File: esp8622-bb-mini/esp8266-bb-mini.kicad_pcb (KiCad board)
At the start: 2 copper layers, 34.3 x 31.8 mm, 17 parts, among them J1 Conn_01x02_Male, J2 Conn_01x04_Male, J3 Conn_01x04_Male, J4 Conn_01x04_Male, J5 Conn_01x04_Male, U1 LP38693MP-3.3, U2 ESP-12F

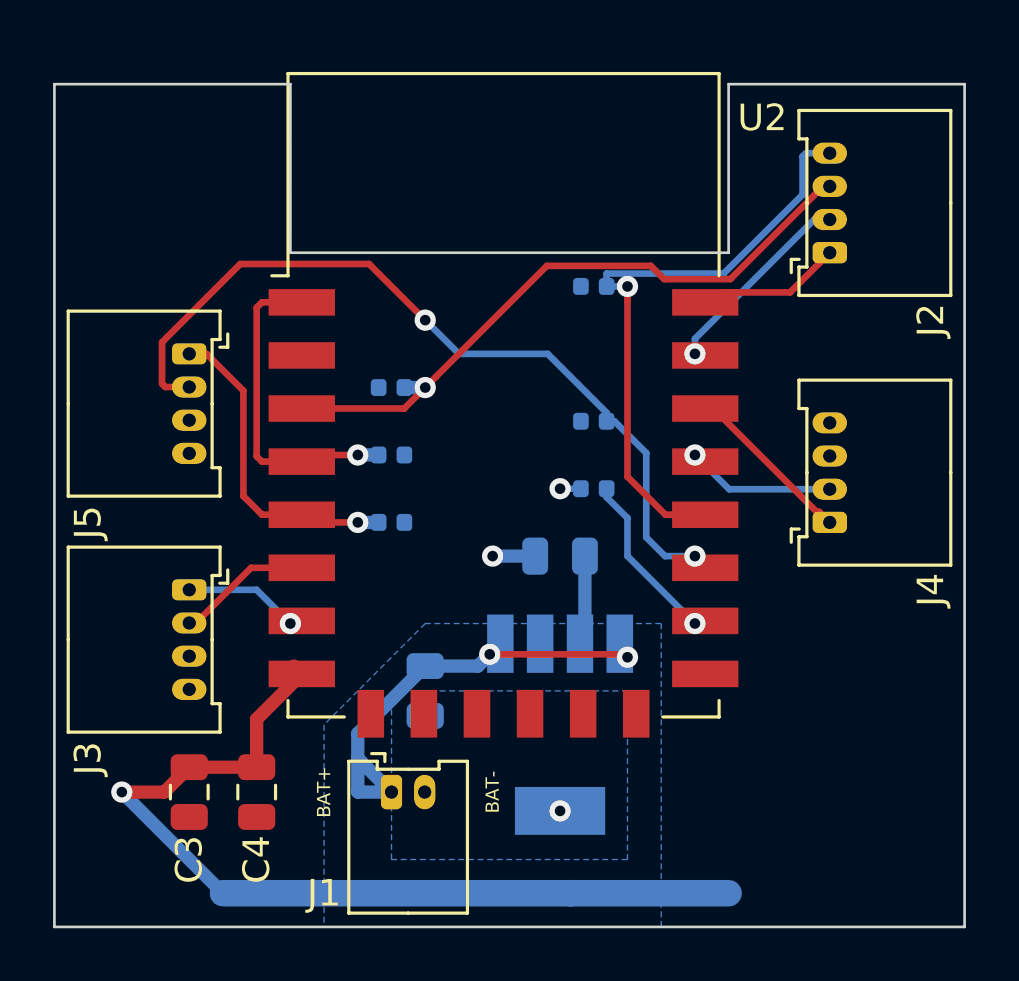
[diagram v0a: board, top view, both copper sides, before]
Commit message: brd: misc changes
- re-add mounting holes
- fix copper pour keepout around input connector
- incooperate voltage divider

Signed-off-by: Tillmann Heidsieck <theidsieck@leenox.de>
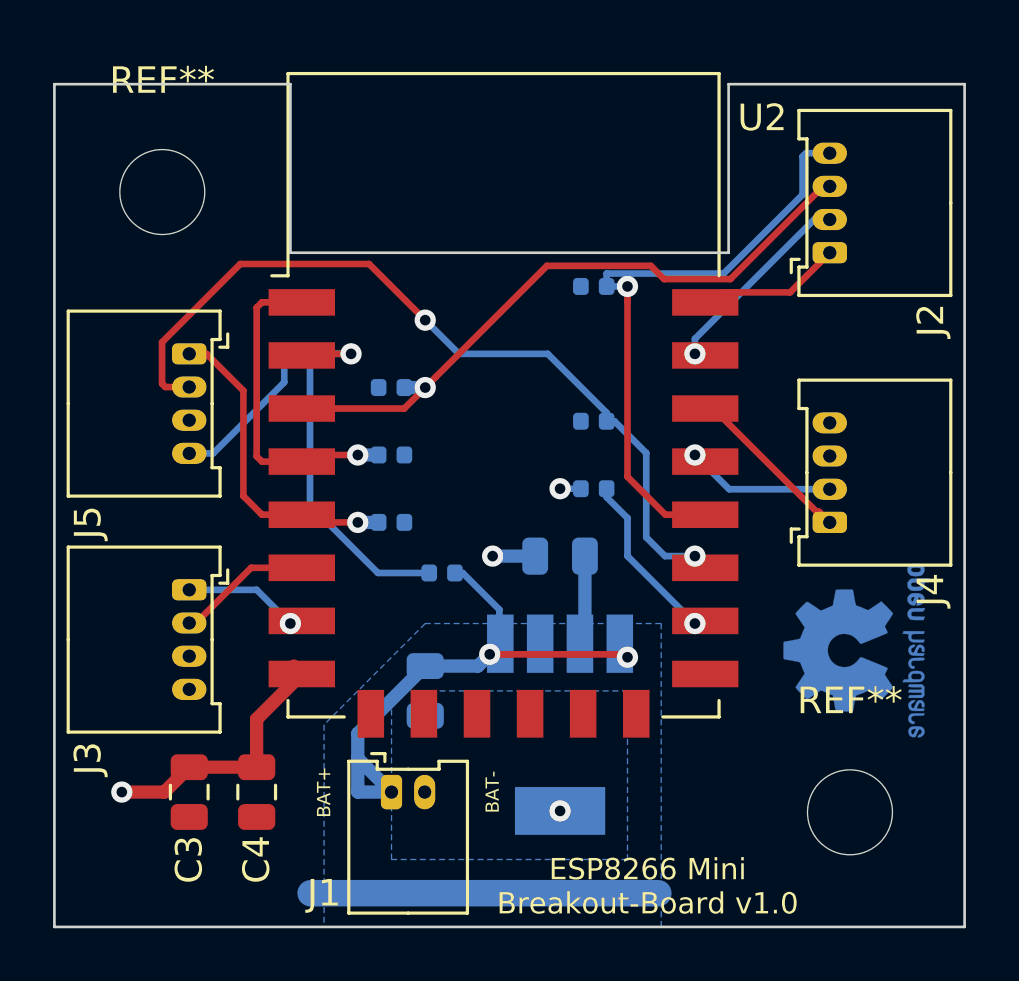
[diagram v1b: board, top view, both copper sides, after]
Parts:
- added R1: 47k, Resistor_SMD:R_0402_1005Metric, B.Cu at (131.4, 104.8)
- added R8: 9k, Resistor_SMD:R_0402_1005Metric, B.Cu at (126.0, 96.5)
- added REF**: OSHW-Logo2_7.3x6mm_Copper, Symbol:OSHW-Logo2_7.3x6mm_Copper, B.Cu at (147.1, 107.7)
- added REF**: MountingHole_3.2mm_M3, MountingHole:MountingHole_3.2mm_M3, F.Cu at (120.9, 90.4)
- added REF**: MountingHole_3.2mm_M3, MountingHole:MountingHole_3.2mm_M3, F.Cu at (146.8, 113.8)
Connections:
- U2 pad 2: Net-(U2-Pad2) -> /ADC_IN
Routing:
- net /ADC_IN: track 0.00 -> 14.7 mm, vias 0 -> 1
- net +3V3: track 38.1 -> 26.8 mm
- net -BATT: track 2.39 -> 8.15 mm
- net +BATT: track 17.3 -> 20.8 mm
